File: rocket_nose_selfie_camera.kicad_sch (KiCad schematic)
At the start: 0 parts

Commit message: sch: add schematic symbols and topology
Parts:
- added D1: PWR_3V3, LED_SMD:LED_0603_1608Metric, symbol Device:LED
- added D2: STATUS, LED_SMD:LED_0603_1608Metric, symbol Device:LED
- added J1: LOGGER TRIGGER / STATUS, Connector_PinHeader_2.54mm:PinHeader_1x03_P2.54mm_Vertical, symbol Connector_Generic:Conn_01x03
- added J2: UART DEBUG (3V3 TTL), Connector_PinHeader_2.54mm:PinHeader_1x04_P2.54mm_Vertical, symbol Connector_Generic:Conn_01x04
- added R1, R3, R4: 1k, Resistor_SMD:R_0603_1608Metric, symbol Device:R
- added R2: 10k, Resistor_SMD:R_0603_1608Metric, symbol Device:R
- added TP1: 5V, TestPoint:TestPoint_Pad_D1.0mm, symbol Connector:TestPoint
- added TP2: 3V3, TestPoint:TestPoint_Pad_D1.0mm, symbol Connector:TestPoint
- added TP3: GND, TestPoint:TestPoint_Pad_D1.0mm, symbol Connector:TestPoint
- added TP4: TRIGGER_IN, TestPoint:TestPoint_Pad_D1.0mm, symbol Connector:TestPoint
- added TP5: STATUS_OUT, TestPoint:TestPoint_Pad_D1.0mm, symbol Connector:TestPoint
- added TP6: UART_TX, TestPoint:TestPoint_Pad_D1.0mm, symbol Connector:TestPoint
- added TP7: UART_RX, TestPoint:TestPoint_Pad_D1.0mm, symbol Connector:TestPoint
- added U1: Seeed Studio XIAO ESP32-S3 Sense, Seeed_Studio_XIAO_Series:XIAO-ESP32-S3-SMD, symbol Seeed_Studio_XIAO_Series:XIAO-ESP32-S3-SMD
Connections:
- new net +3V3: J2.4 (Pin_4), R3.1, TP2.1, U1.12 (3V3_OUT)
- new net +5V: TP1.1, U1.14 (VBUS)
- new net GND: D1.1 (K), D2.1 (K), J1.2 (Pin_2), J2.1 (Pin_1), R2.2, TP3.1, U1.13 (GND), U1.18 (GND), U1.24 (GND), U1.25 (PAD)
- new net PWR_LED_A: D1.2 (A), R3.2
- new net STATUS_LED_A: D2.2 (A), R4.2
- new net STATUS_OUT: J1.3 (Pin_3), R4.1, TP5.1, U1.2 (D1)
- new net TRIGGER_IN: R1.2, R2.1, TP4.1, U1.1 (D0)
- new net TRIGGER_IN_EXT: J1.1 (Pin_1), R1.1
- new net UART_RX: J2.3 (Pin_3), TP7.1, U1.8 (D7)
- new net UART_TX: J2.2 (Pin_2), TP6.1, U1.7 (D6)

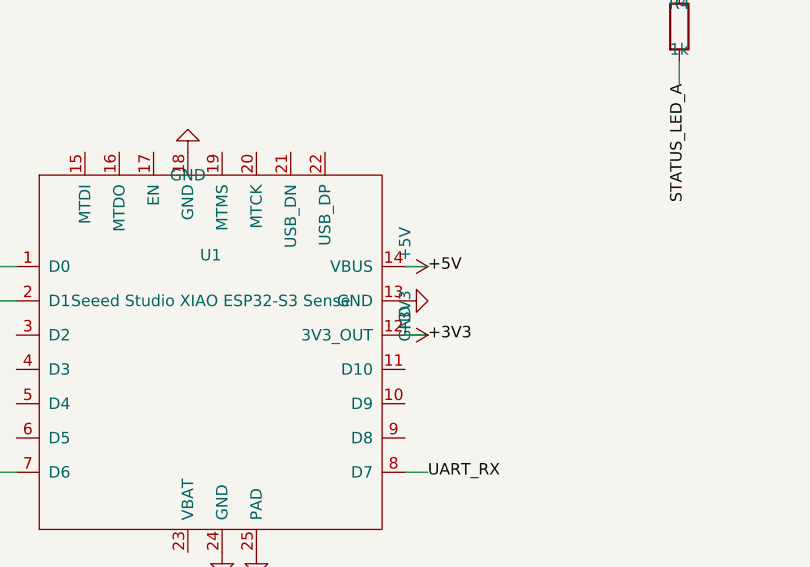
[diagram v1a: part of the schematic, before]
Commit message: sch: validate power flags
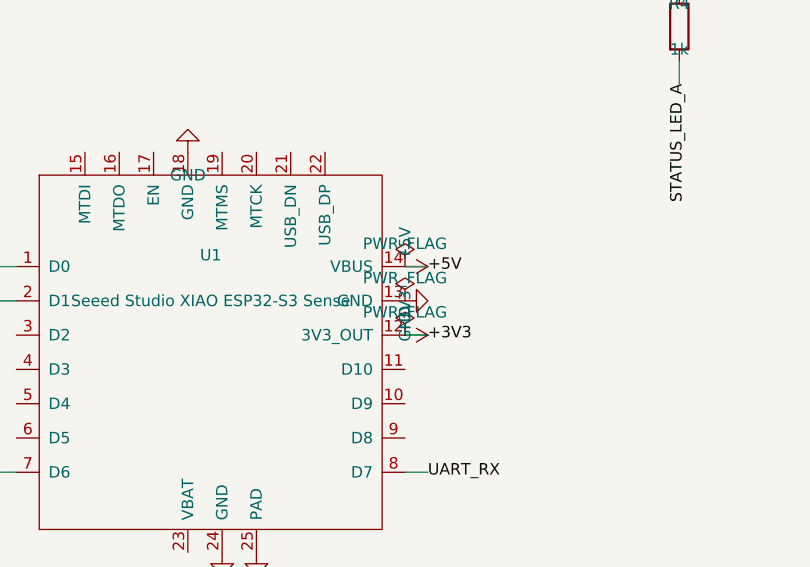
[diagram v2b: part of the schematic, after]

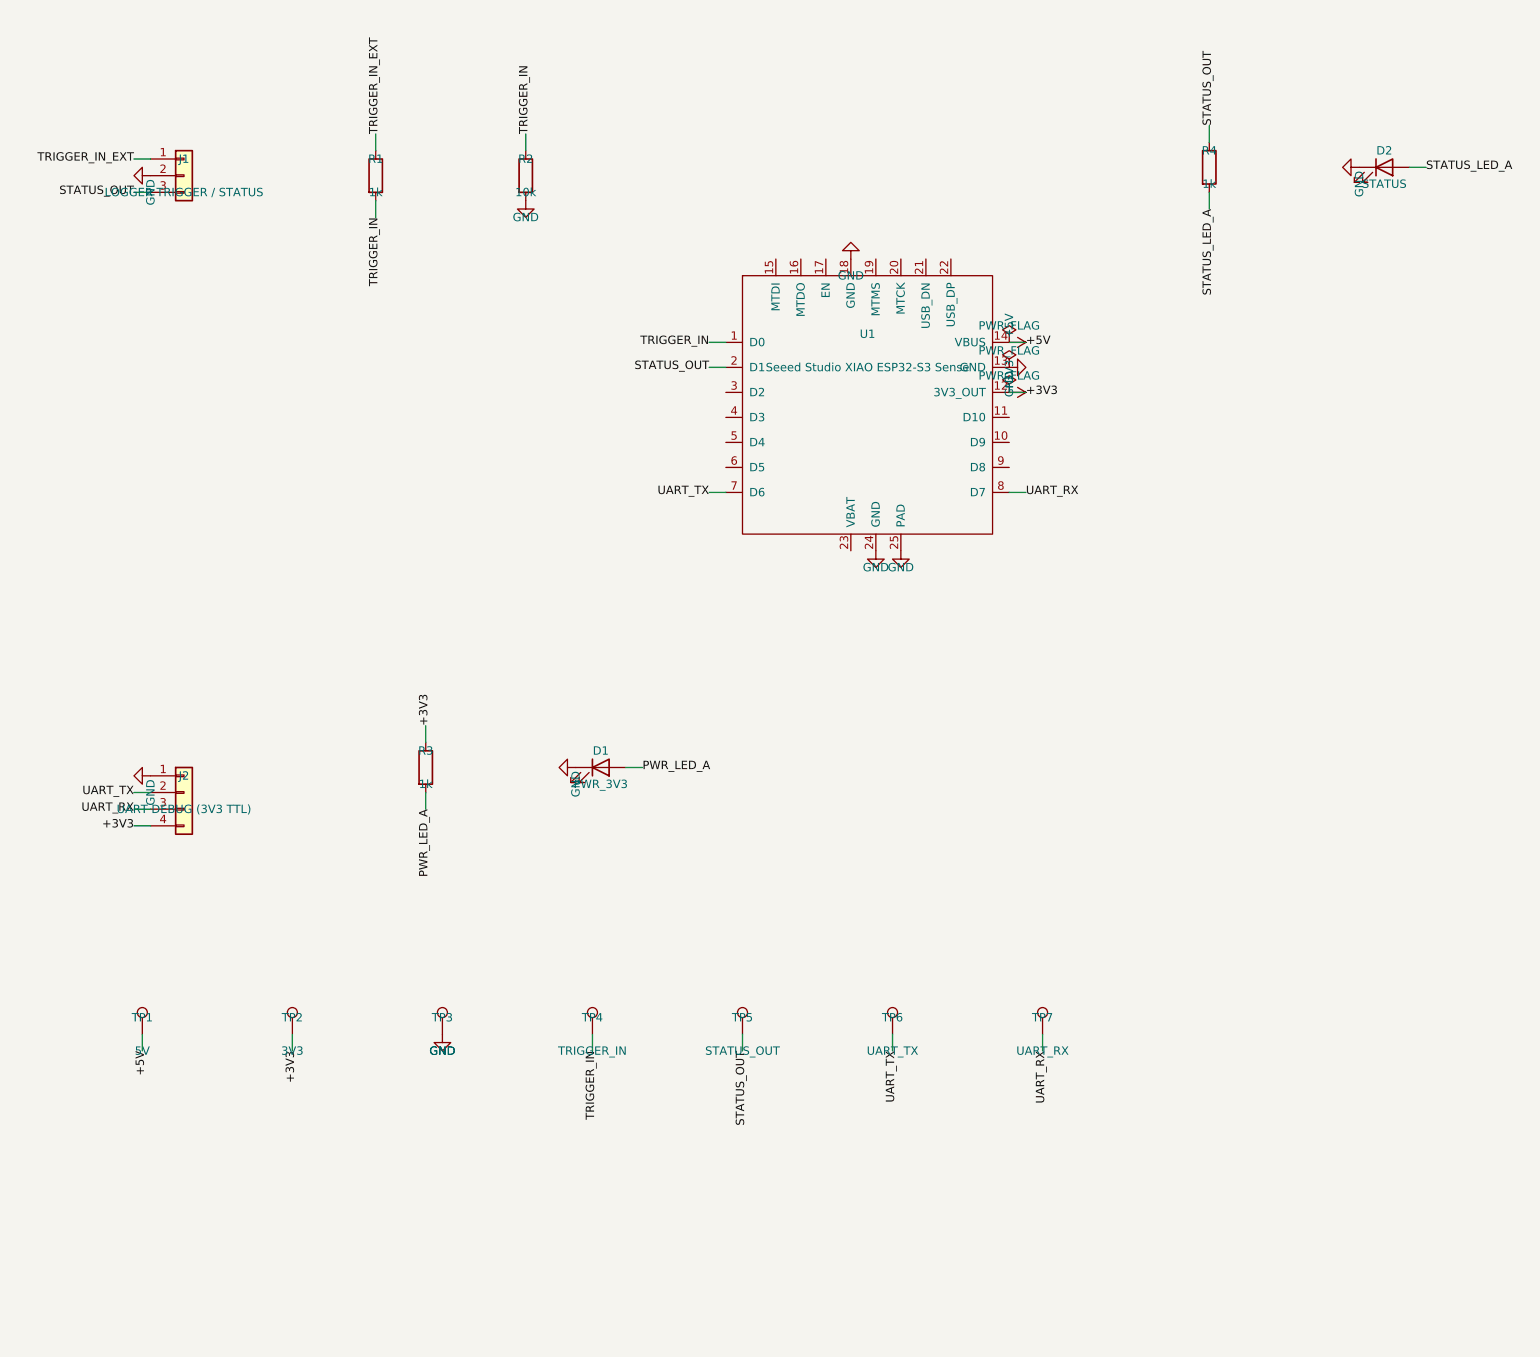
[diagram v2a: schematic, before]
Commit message: sch: complete schematic presentation
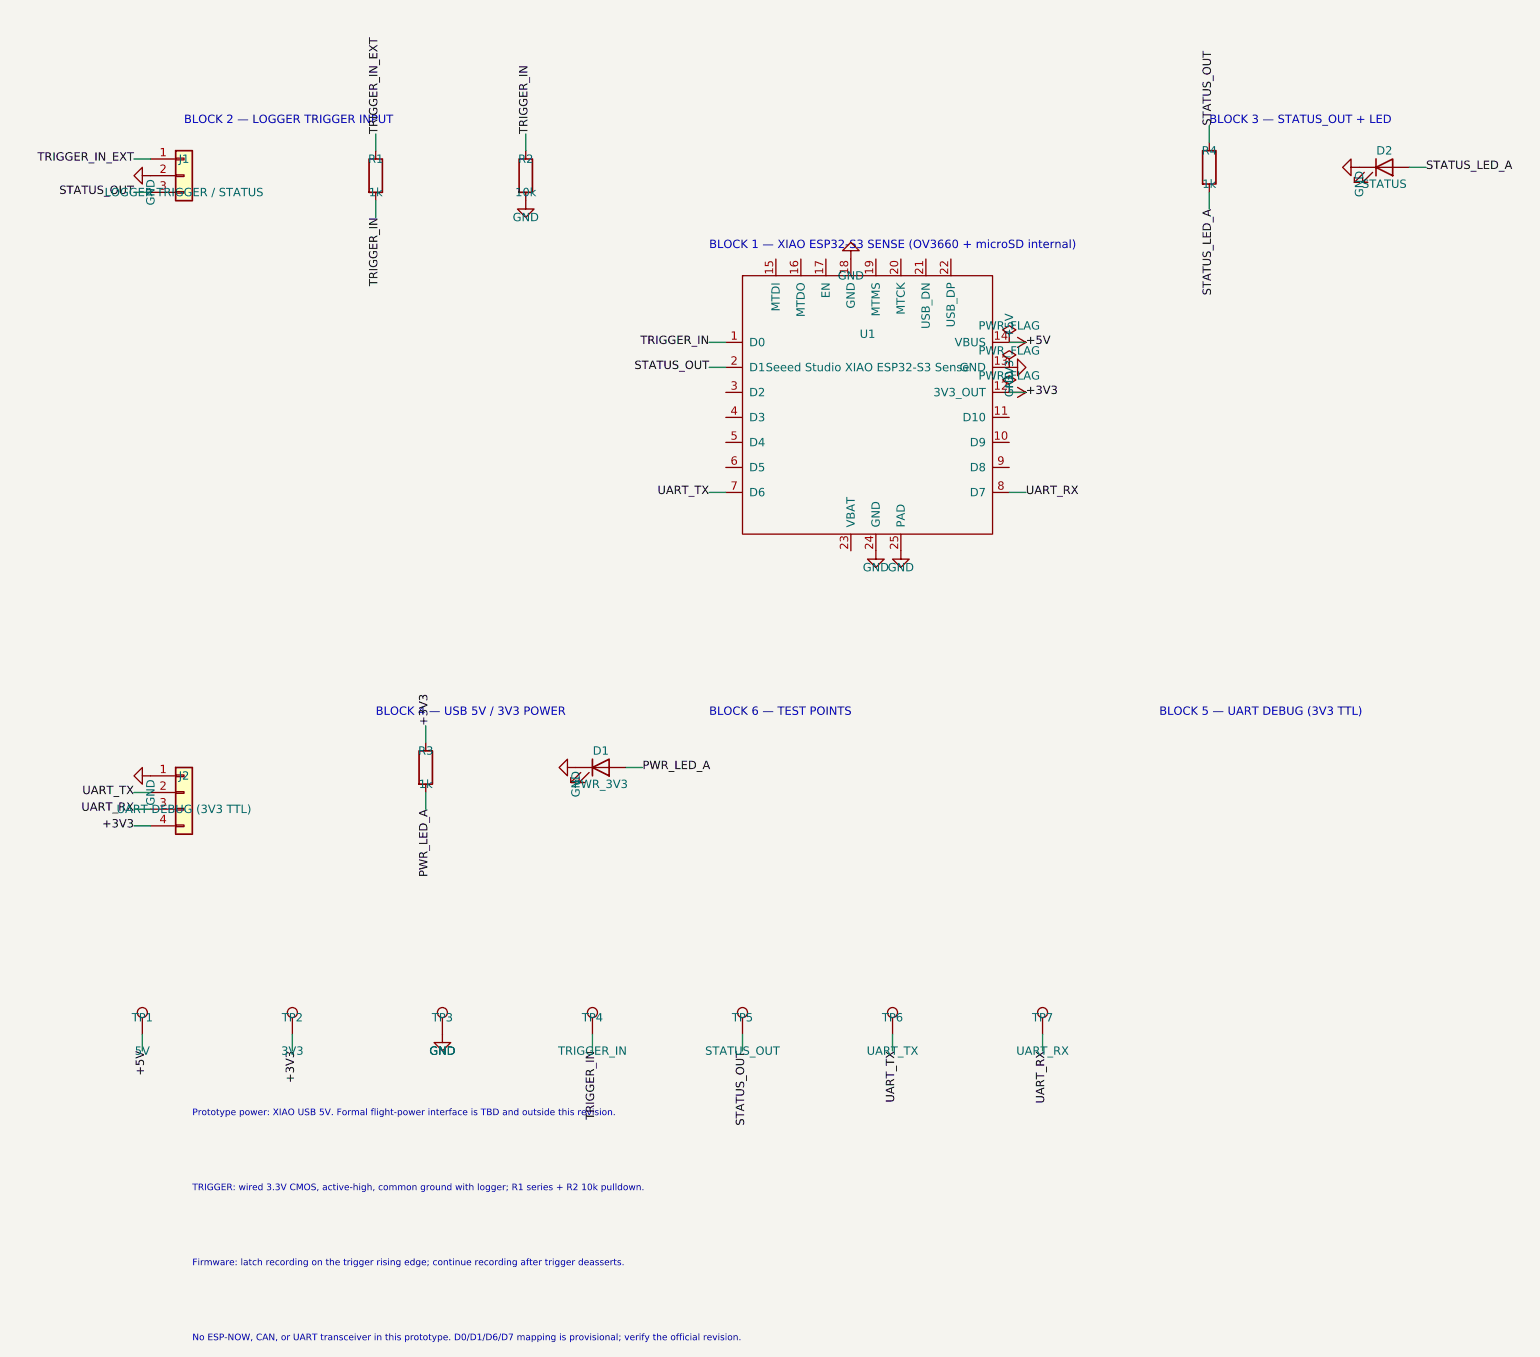
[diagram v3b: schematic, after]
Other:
- note added: "BLOCK 1 — XIAO ESP32-S3 SENSE (OV3660 + microSD internal)"
- note added: "BLOCK 2 — LOGGER TRIGGER INPUT"
- note added: "BLOCK 3 — STATUS_OUT + LED"
- note added: "BLOCK 4 — USB 5V / 3V3 POWER"
- note added: "BLOCK 5 — UART DEBUG (3V3 TTL)"
- note added: "BLOCK 6 — TEST POINTS"
- note added: "Firmware: latch recording on the trigger rising edge; continue recording after trigger deasserts."
- note added: "No ESP-NOW, CAN, or UART transceiver in this prototype. D0/D1/D6/D7 mapping is provisional; verify the official revision."
- note added: "Prototype power: XIAO USB 5V. Formal flight-power interface is TBD and outside this revision."
- note added: "TRIGGER: wired 3.3V CMOS, active-high, common ground with logger; R1 series + R2 10k pulldown."
